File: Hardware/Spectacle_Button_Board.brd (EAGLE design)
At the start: 44.5 x 73.7 mm, 50 parts, among them J17 AUDIO-JACK3, J19 FTDI_DEVICE, J20 AUDIO-JACK3, U1 CY8C4146LQI-S422, U2 3.3V/150mA

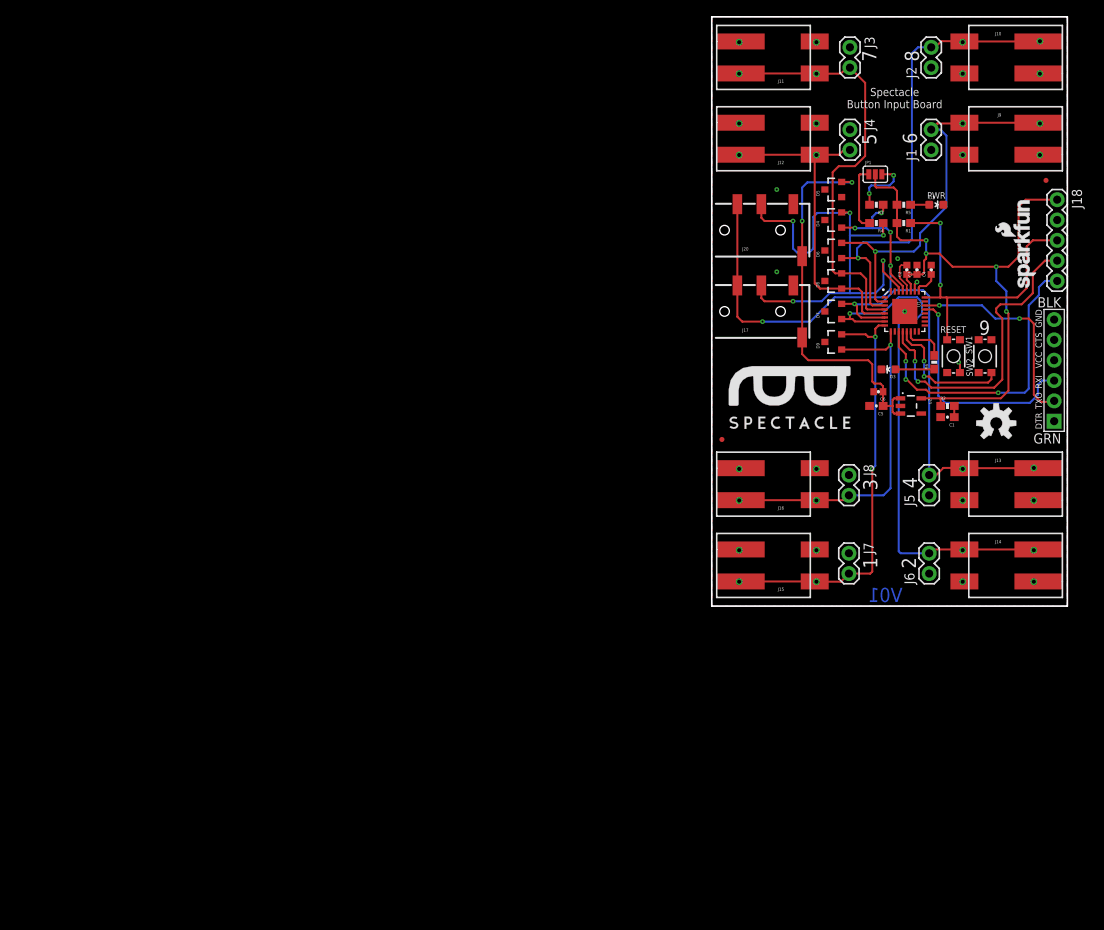
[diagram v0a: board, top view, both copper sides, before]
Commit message: Added circuitry for downstream power control
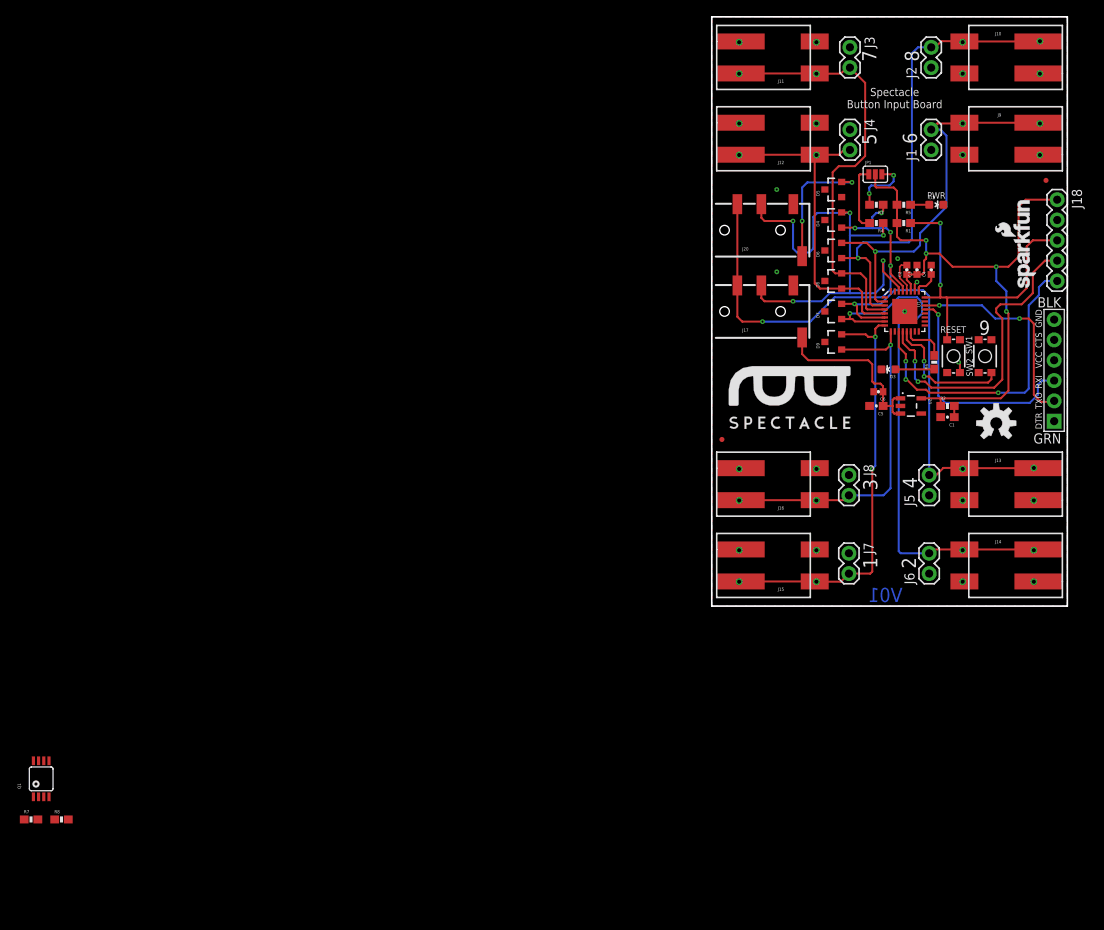
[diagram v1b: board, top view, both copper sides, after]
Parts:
- added Q1: (no value), SparkFun-DiscreteSemi:MSOP8
- added R7, R8: 10K, SparkFun-Resistors:0603-RES
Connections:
- new net N$26: Q1.4, Q1.7, Q1.8, R8.1
- new net VOUT: D5.2, J20.EARTH, Q1.5, Q1.6
- new net V_OUT_EN: Q1.2, R7.1, U1.17
- net GND: now also Q1.1, R7.2
- net VIN: now also D5.1, Q1.3, R8.2; no longer D5.2, J20.EARTH
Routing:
- net VIN: track 49.0 -> 22.4 mm, vias 2 -> 0
- net VOUT: track 0.00 -> 16.4 mm, vias 0 -> 2

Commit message: Revised for downstream power circuit
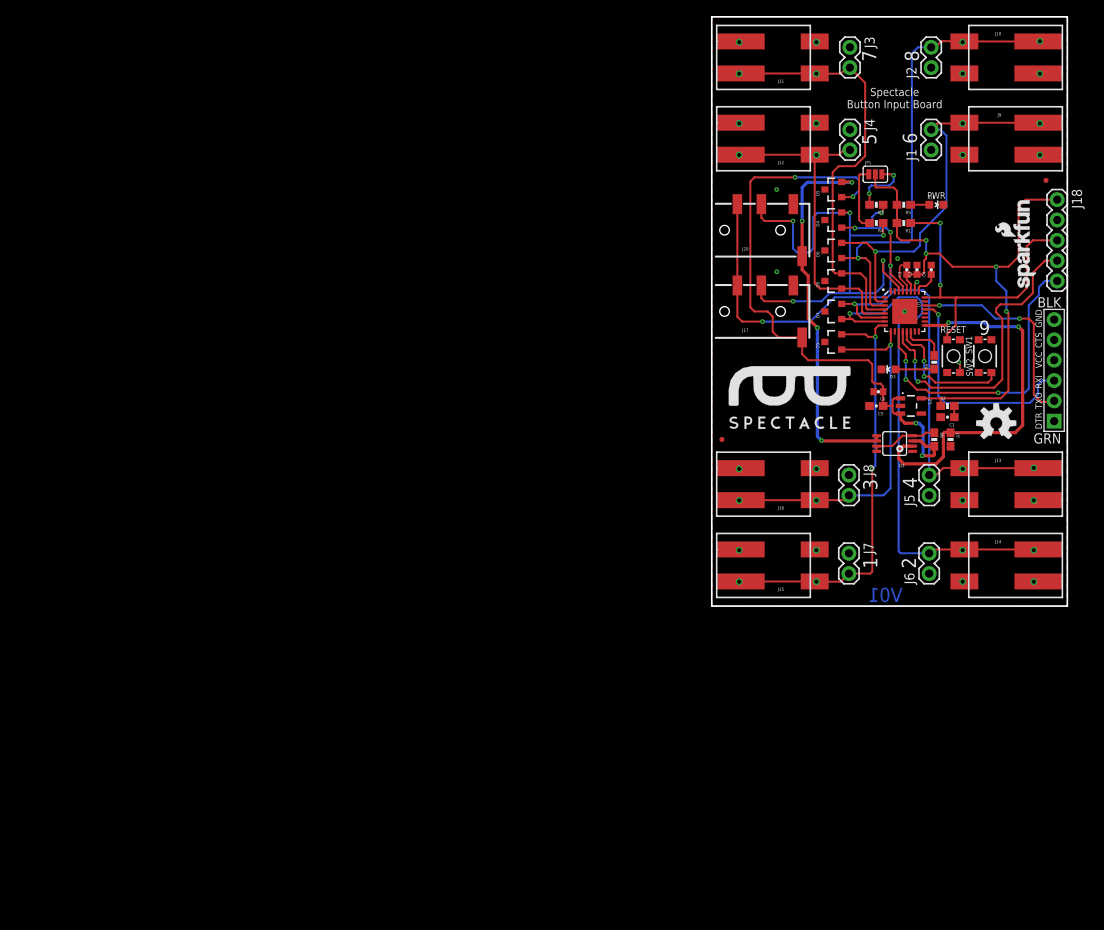
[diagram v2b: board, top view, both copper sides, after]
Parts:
- moved R7 124.4 mm to (29.8, 20.8), turned to 270 degrees
- moved R8 119.0 mm to (27.8, 20.8), turned to 270 degrees
- moved Q1 114.6 mm to (22.9, 20.3), turned to 90 degrees
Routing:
- net VIN: track 22.4 -> 78.2 mm, vias 0 -> 4
- net V_OUT_EN: track 0.00 -> 47.1 mm, vias 0 -> 2
- net VOUT: track 16.4 -> 48.0 mm, vias 2 -> 4
- net N$26: track 0.00 -> 8.55 mm

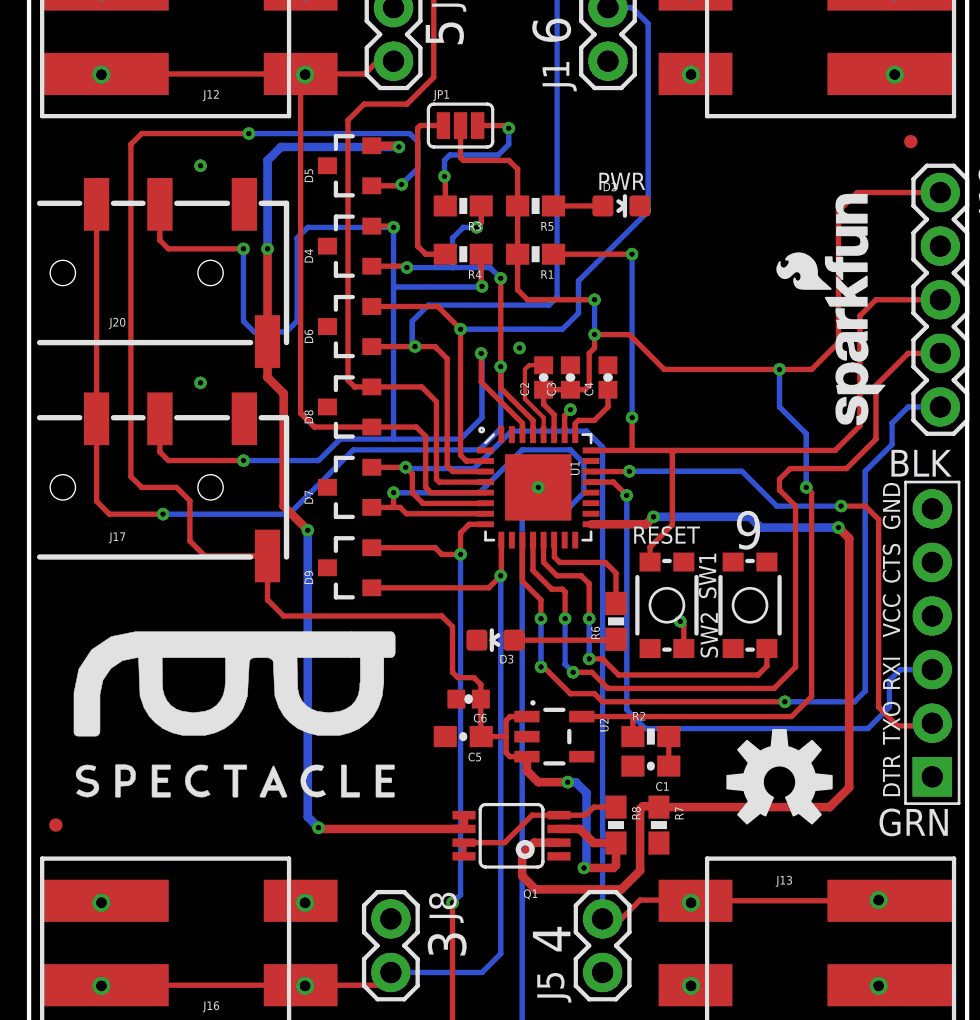
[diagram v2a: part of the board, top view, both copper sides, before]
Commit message: Fixed VIN and VOUT lines
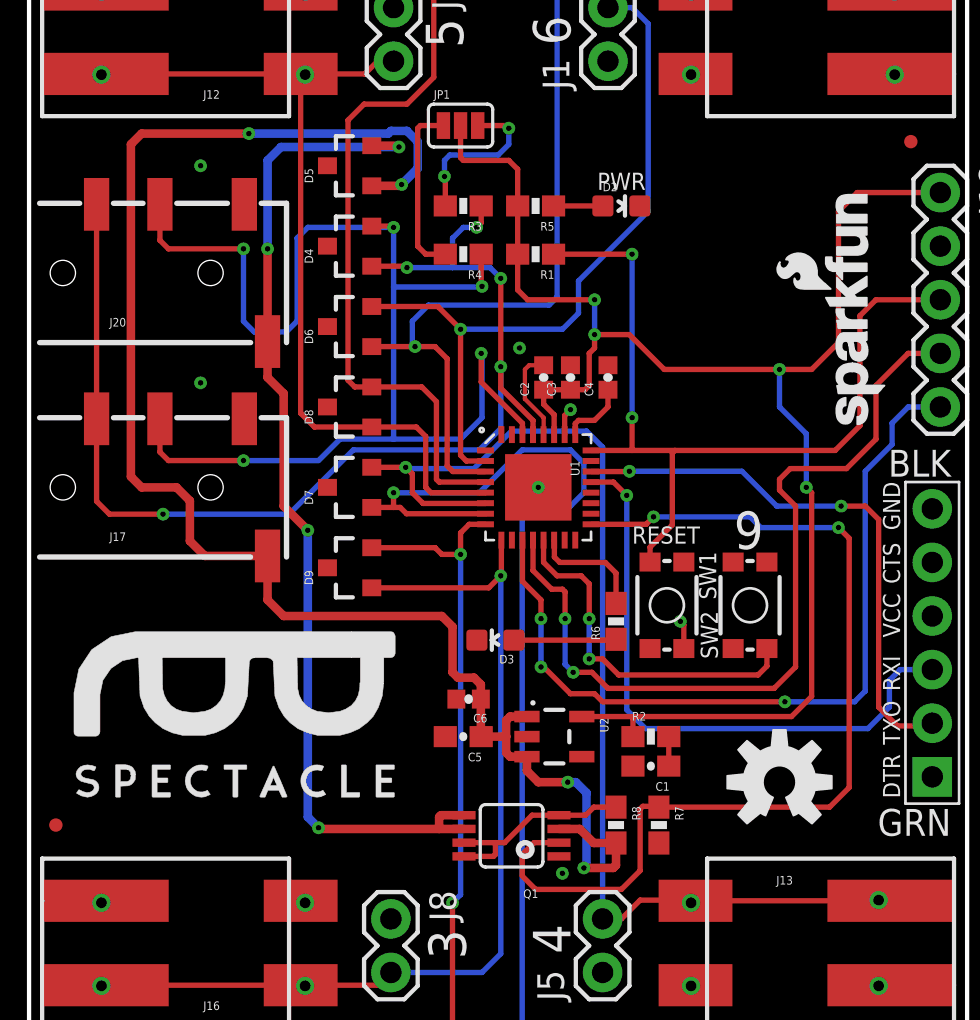
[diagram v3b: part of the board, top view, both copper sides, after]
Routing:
- net N$26: track 8.55 -> 9.99 mm
- net VOUT: track 48.0 -> 49.1 mm
- net GND: vias 22 -> 23

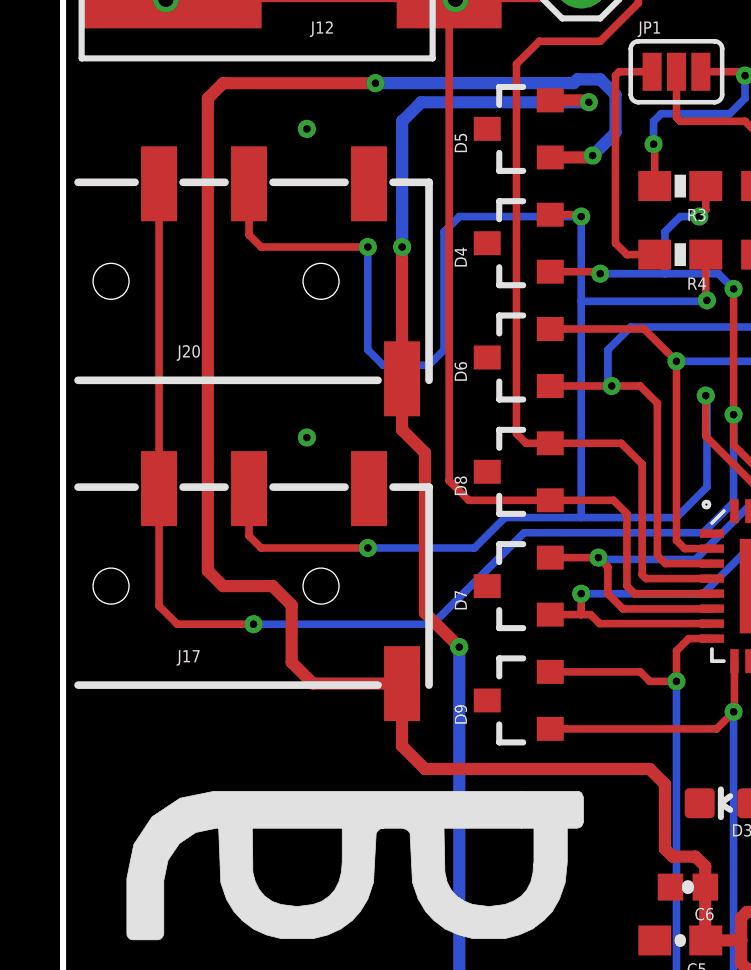
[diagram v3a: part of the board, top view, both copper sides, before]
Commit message: added input and output silk
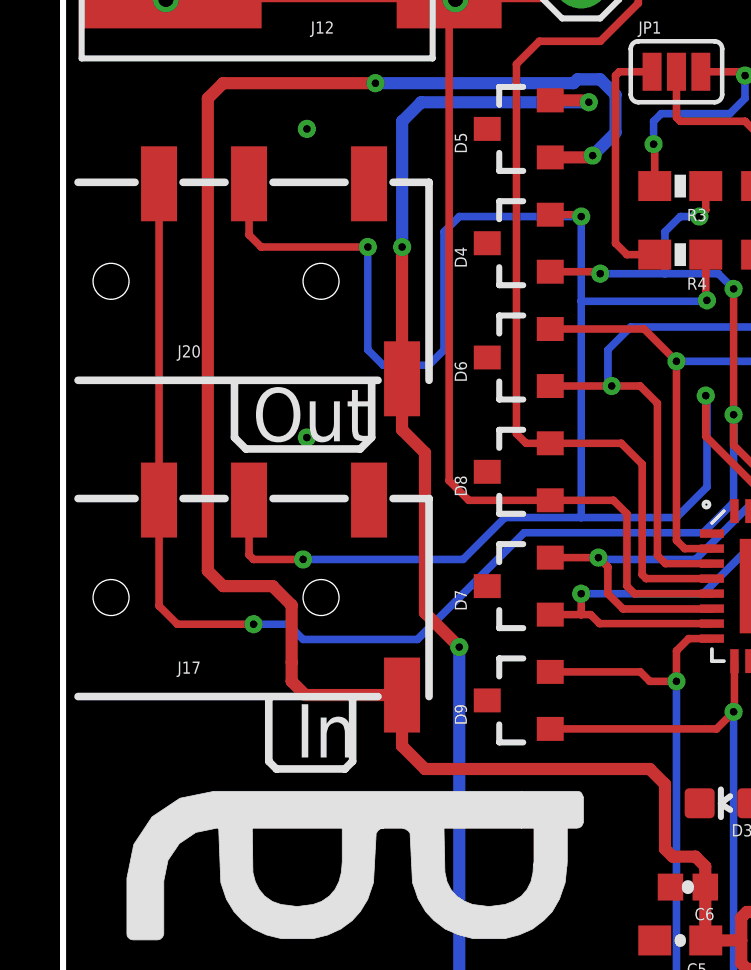
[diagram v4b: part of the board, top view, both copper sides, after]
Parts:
- moved J17 0.38 mm to (0.00, 36.4)
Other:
- board text added: "In"
- board text added: "Out"
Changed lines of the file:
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@@
 <rectangle x1="23.87" y1="34.91" x2="24.39" y2="35.26" layer="41"/>
 <rectangle x1="25.7" y1="36.56" x2="26.04" y2="37.1" layer="41"/>
+<text x="9.779" y="32.893" size="1.778" layer="21" font="vector" ratio="15" rot="R180">In</text>
+<text x="10.287" y="43.434" size="1.778" layer="21" font="vector" ratio="15" rot="R180">Out</text>
+<wire x1="5.715" y1="43.561" x2="5.715" y2="41.783" width="0.254" layer="21"/>
+<wire x1="5.715" y1="41.783" x2="6.096" y2="41.402" width="0.254" layer="21"/>
+<wire x1="6.858" y1="33.02" x2="6.858" y2="30.988" width="0.254" layer="21"/>
+<wire x1="6.858" y1="30.988" x2="7.112" y2="30.734" width="0.254" layer="21"/>
+<wire x1="9.652" y1="33.02" x2="9.652" y2="30.988" width="0.254" layer="21"/>
+<wire x1="9.652" y1="30.988" x2="9.398" y2="30.734" width="0.254" layer="21"/>
+<wire x1="9.398" y1="30.734" x2="7.112" y2="30.734" width="0.254" layer="21"/>
+<wire x1="10.287" y1="43.561" x2="10.287" y2="41.783" width="0.254" layer="21"/>
+<wire x1="10.287" y1="41.783" x2="9.906" y2="41.402" width="0.254" layer="21"/>
+<wire x1="9.906" y1="41.402" x2="6.096" y2="41.402" width="0.254" layer="21"/>
 </plain>
 <attributes>
@@
 <attribute name="PROD_ID" value="RES-07856" x="27.813" y="30.48" size="1.778" layer="27" font="vector" ratio="15" rot="R90" display="off"/>
 </element>
-<element name="J17" library="SparkFun-Connectors" package="AUDIO-JACK-TRRS-SMD" value="AUDIO-JACK3" x="0" y="36.83">
-<attribute name="PROD_ID" value="CONN-10676" x="0" y="36.83" size="1.778" layer="27" display="off"/>
+<element name="J17" library="SparkFun-Connectors" package="AUDIO-JACK-TRRS-SMD" value="AUDIO-JACK3" x="0" y="36.449">
+<attribute name="PROD_ID" value="CONN-10676" x="0" y="36.449" size="1.778" layer="27" display="off"/>
 </element>
 <element name="D4" library="SparkFun-DiscreteSemi" package="SOT23-3" value="PESD1CAN" x="15.24" y="48.26" rot="R90">
@@
 <wire x1="19.558" y1="30.734" x2="12.065" y2="30.734" width="0.4064" layer="1"/>
 <wire x1="12.065" y1="30.734" x2="11.3" y2="31.499" width="0.4064" layer="1"/>
-<wire x1="11.3" y1="33.58" x2="11.3" y2="31.499" width="0.4064" layer="1"/>
+<wire x1="11.3" y1="33.199" x2="11.3" y2="31.499" width="0.4064" layer="1"/>
 <contactref element="Q1" pad="3"/>
 <contactref element="R8" pad="2"/>
@@
 <wire x1="16.24" y1="51.12" x2="17.592" y2="51.12" width="0.4064" layer="1"/>
 <wire x1="17.592" y1="51.12" x2="17.653" y2="51.181" width="0.254" layer="1"/>
-<wire x1="11.3" y1="33.58" x2="8.33" y2="33.58" width="0.4064" layer="1"/>
-<wire x1="8.33" y1="33.58" x2="7.62" y2="34.29" width="0.4064" layer="1"/>
 <wire x1="7.62" y1="34.29" x2="7.62" y2="36.195" width="0.4064" layer="1"/>
 <wire x1="7.62" y1="36.195" x2="6.985" y2="36.83" width="0.4064" layer="1"/>
@@
 <wire x1="27.686" y1="18.796" x2="27.813" y2="18.923" width="0.4064" layer="1"/>
 <wire x1="27.813" y1="19.978" x2="27.813" y2="18.923" width="0.4064" layer="1"/>
+<wire x1="11.3" y1="33.199" x2="8.076" y2="33.199" width="0.4064" layer="1"/>
+<wire x1="8.076" y1="33.199" x2="7.62" y2="33.655" width="0.4064" layer="1"/>
+<wire x1="7.62" y1="33.655" x2="7.62" y2="34.29" width="0.4064" layer="1"/>
 </signal>
 <signal name="N$2">
@@
 <wire x1="22.352" y1="46.736" x2="22.352" y2="42.545" width="0.254" layer="1"/>
 <wire x1="22.352" y1="42.545" x2="22.352" y2="41.529" width="0.254" layer="1"/>
-<wire x1="12.319" y1="35.56" x2="15.367" y2="38.608" width="0.254" layer="16"/>
 <wire x1="15.367" y1="38.608" x2="21.336" y2="38.608" width="0.254" layer="16"/>
 <wire x1="21.336" y1="38.608" x2="22.352" y2="39.624" width="0.254" layer="16"/>
@@
 <via x="22.352" y="42.545" extent="1-16" drill="0.254"/>
 <via x="6.35" y="35.56" extent="1-16" drill="0.254"/>
-<wire x1="6.35" y1="35.56" x2="12.319" y2="35.56" width="0.254" layer="16"/>
 <wire x1="22.352" y1="46.736" x2="21.844" y2="47.244" width="0.254" layer="16"/>
 <wire x1="21.844" y1="47.244" x2="20.066" y2="47.244" width="0.254" layer="16"/>
@@
 <contactref element="J20" pad="RING2"/>
 <contactref element="R3" pad="1"/>
-<wire x1="3.2" y1="40.08" x2="3.2" y2="36.17" width="0.254" layer="1"/>
+<wire x1="3.2" y1="39.699" x2="3.2" y2="36.17" width="0.254" layer="1"/>
 <wire x1="3.2" y1="36.17" x2="3.81" y2="35.56" width="0.254" layer="1"/>
-<wire x1="6.35" y1="35.56" x2="3.81" y2="35.56" width="0.254" layer="1"/>
-<wire x1="3.2" y1="40.08" x2="3.2" y2="50.24" width="0.254" layer="1"/>
+<wire x1="3.2" y1="39.699" x2="3.2" y2="50.24" width="0.254" layer="1"/>
 <wire x1="21.424" y1="50.165" x2="21.424" y2="49.364" width="0.254" layer="1"/>
 <wire x1="21.424" y1="49.364" x2="21.209" y2="49.149" width="0.254" layer="1"/>
 <wire x1="16.24" y1="47.31" x2="17.841" y2="47.31" width="0.254" layer="1"/>
 <wire x1="17.841" y1="47.31" x2="17.907" y2="47.244" width="0.254" layer="1"/>
+<wire x1="3.81" y1="35.56" x2="6.35" y2="35.56" width="0.254" layer="1"/>
+<wire x1="6.35" y1="35.56" x2="7.493" y2="35.56" width="0.254" layer="16"/>
+<wire x1="7.493" y1="35.56" x2="8.001" y2="35.052" width="0.254" layer="16"/>
+<wire x1="8.001" y1="35.052" x2="11.811" y2="35.052" width="0.254" layer="16"/>
+<wire x1="11.811" y1="35.052" x2="15.367" y2="38.608" width="0.254" layer="16"/>
 </signal>
 <signal name="SDA">
@@
 <wire x1="21.424" y1="43.18" x2="21.424" y2="41.822" width="0.254" layer="1"/>
 <wire x1="21.424" y1="41.822" x2="23.38" y2="39.866" width="0.254" layer="1"/>
-<wire x1="10.2" y1="38.14" x2="10.16" y2="38.1" width="0.254" layer="1"/>
-<via x="10.16" y="38.1" extent="1-16" drill="0.254"/>
-<wire x1="10.16" y1="38.1" x2="13.716" y2="38.1" width="0.254" layer="16"/>
-<wire x1="13.716" y1="38.1" x2="14.732" y2="39.116" width="0.254" layer="16"/>
 <wire x1="14.732" y1="39.116" x2="17.272" y2="39.116" width="0.254" layer="16"/>
 <wire x1="17.272" y1="39.116" x2="20.447" y2="39.116" width="0.254" layer="16"/>
@@
 <contactref element="J17" pad="RING1"/>
 <contactref element="R4" pad="1"/>
-<wire x1="10.16" y1="38.1" x2="6.604" y2="38.1" width="0.254" layer="1"/>
-<wire x1="6.604" y1="38.1" x2="6.2" y2="38.504" width="0.254" layer="1"/>
-<wire x1="6.2" y1="40.08" x2="6.2" y2="38.504" width="0.254" layer="1"/>
 <wire x1="10.16" y1="48.133" x2="6.604" y2="48.133" width="0.254" layer="1"/>
 <wire x1="6.604" y1="48.133" x2="6.2" y2="48.537" width="0.254" layer="1"/>
@@
 <wire x1="21.424" y1="47.879" x2="21.424" y2="46.394" width="0.254" layer="1"/>
 <wire x1="21.424" y1="46.394" x2="21.463" y2="46.355" width="0.254" layer="1"/>
+<via x="8.001" y="37.719" extent="1-16" drill="0.254"/>
+<wire x1="8.001" y1="37.719" x2="6.35" y2="37.719" width="0.254" layer="1"/>
+<wire x1="6.35" y1="37.719" x2="6.2" y2="37.869" width="0.254" layer="1"/>
+<wire x1="6.2" y1="39.699" x2="6.2" y2="37.869" width="0.254" layer="1"/>
+<wire x1="8.001" y1="37.719" x2="13.335" y2="37.719" width="0.254" layer="16"/>
+<wire x1="13.335" y1="37.719" x2="14.732" y2="39.116" width="0.254" layer="16"/>
 </signal>
 <signal name="N$6">
